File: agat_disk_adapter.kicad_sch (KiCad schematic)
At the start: 14 parts, among them J1 КОНТРОЛЛЕР, J2_A1 ИЗОТ, J2_B2 ИЗОТ, J3 DISK II, J4 GOTEK, J5 Питание GOTEK, J6 ВБ, J7 Джамперы, J8 ВБ2, J9_A1 КОНТРОЛЛЕР, J9_B2 КОНТРОЛЛЕР

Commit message: add second FDC connector - Eltra male for standard Agat FDD cable
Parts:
- removed R2: 0, Resistor_SMD:R_1206_3216Metric, symbol Device:R
- added J9: PIN_32, Connector_PinHeader_2.54mm:PinHeader_1x02_P2.54mm_Horizontal, symbol Connector:Conn_01x02_Pin
- renumbered R3 to R2
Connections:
- net PH1: now also J9.2 (Pin_2)
- net PIN_32: now reaches J4.32 (Pin_32), R2.2
- net PIN_32: now also J9.1 (Pin_1)
- net DS2 renamed DE2
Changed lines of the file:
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@@
 	)
 	(junction
+		(at 91.44 175.26)
+		(diameter 0)
+		(color 0 0 0 0)
+	)
+	(junction
 		(at 91.44 106.68)
 		(diameter 0)
@@
 	)
 	(junction
-		(at 91.44 166.878)
-		(diameter 0)
-		(color 0 0 0 0)
-	)
-	(junction
 		(at 81.28 191.643)
 		(diameter 0)
@@
 	(wire
 		(pts
-			(xy 91.44 166.878) (xy 91.44 177.038)
+			(xy 91.44 166.878) (xy 91.44 175.26)
 		)
 		(stroke
@@
 	(wire
 		(pts
+			(xy 91.44 175.26) (xy 91.44 177.038)
+		)
+		(stroke
+			(width 0)
+			(type default)
+		)
+	)
+	(wire
+		(pts
 			(xy 60.96 191.643) (xy 60.96 189.738)
 		)
@@
 	(wire
 		(pts
+			(xy 106.68 180.34) (xy 106.68 175.26)
+		)
+		(stroke
+			(width 0)
+			(type default)
+		)
+	)
+	(wire
+		(pts
 			(xy 78.74 18.415) (xy 78.74 25.4)
 		)
@@
 	(wire
 		(pts
+			(xy 91.44 175.26) (xy 104.14 175.26)
+		)
+		(stroke
+			(width 0)
+			(type default)
+		)
+	)
+	(wire
+		(pts
 			(xy 29.21 37.465) (xy 29.21 34.925)
 		)
@@
 		)
 	)
+	(label "PIN_32"
+		(at 91.948 175.26 0)
+		(effects
+			(font
+				(size 1.27 1.27)
+			)
+			(justify left bottom)
+		)
+	)
 	(label "EN1"
 		(at 78.74 66.675 270)
@@
 		)
 	)
-	(label "+5"
-		(at 80.518 166.878 0)
+	(label "PH1"
+		(at 106.68 180.34 0)
 		(effects
 			(font
@@
 		)
 	)
-	(label "DS2"
+	(label "DE2"
 		(at 99.06 121.285 90)
 		(effects
@@
 	)
 	(symbol
-		(lib_id "Device:R")
-		(at 87.63 166.878 90)
-		(unit 1)
-		(body_style 1)
-		(exclude_from_sim no)
-		(in_bom yes)
-		(on_board yes)
-		(in_pos_files yes)
-		(dnp no)
-		(property "Reference" "R2"
-			(at 86.36 164.592 90)
-			(show_name no)
-			(do_not_autoplace no)
-			(effects
-				(font
-					(size 1.27 1.27)
-				)
-			)
-		)
-		(property "Value" "0"
-			(at 89.662 164.592 90)
-			(show_name no)
-			(do_not_autoplace no)
-			(effects
-				(font
-					(size 1.27 1.27)
-				)
-			)
-		)
-		(property "Footprint" "Resistor_SMD:R_1206_3216Metric"
-			(at 87.63 168.656 90)
-			(hide yes)
-			(show_name no)
-			(do_not_autoplace no)
-			(effects
-				(font
-					(size 1.27 1.27)
-				)
-			)
-		)
-		(property "Datasheet" ""
-			(at 87.63 166.878 0)
-			(hide yes)
-			(show_name no)
-			(do_not_autoplace no)
-			(effects
-				(font
-					(size 1.27 1.27)
-				)
-			)
-		)
-		(property "Description" "Resistor"
-			(at 87.63 166.878 0)
-			(hide yes)
-			(show_name no)
-			(do_not_autoplace no)
-			(effects
-				(font
-					(size 1.27 1.27)
-				)
-			)
-		)
-		(pin "2"
-		)
-		(pin "1"
-		)
-		(instances
-			(project "agat_disk_adapter"
-				(path "/e6908ff4-84b7-4cdb-b4c1-fd2e829eca09"
-					(reference "R2")
-					(unit 1)
-				)
-			)
-		)
-	)
-	(symbol
 		(lib_id "power:GND")
 		(at 95.885 38.1 0)
@@
 	)
 	(symbol
+		(lib_id "Connector:Conn_01x02_Pin")
+		(at 104.14 170.18 90)
+		(mirror x)
+		(unit 1)
+		(body_style 1)
+		(exclude_from_sim no)
+		(in_bom yes)
+		(on_board yes)
+		(in_pos_files yes)
+		(dnp no)
+		(property "Reference" "J9"
+			(at 100.838 172.212 90)
+			(show_name no)
+			(do_not_autoplace no)
+			(effects
+				(font
+					(size 1.27 1.27)
+				)
+				(justify right)
+			)
+		)
+		(property "Value" "PIN_32"
+			(at 92.202 175.006 90)
+			(hide yes)
+			(show_name no)
+			(do_not_autoplace no)
+			(effects
+				(font
+					(size 1.27 1.27)
+				)
+				(justify right)
+			)
+		)
+		(property "Footprint" "Connector_PinHeader_2.54mm:PinHeader_1x02_P2.54mm_Horizontal"
+			(at 104.14 170.18 0)
+			(hide yes)
+			(show_name no)
+			(do_not_autoplace no)
+			(effects
+				(font
+					(size 1.27 1.27)
+				)
+			)
+		)
+		(property "Datasheet" ""
+			(at 104.14 170.18 0)
+			(hide yes)
+			(show_name no)
+			(do_not_autoplace no)
+			(effects
+				(font
+					(size 1.27 1.27)
+				)
+			)
+		)
+		(property "Description" "Generic connector, single row, 01x02, script generated"
+			(at 104.14 170.18 0)
+			(hide yes)
+			(show_name no)
+			(do_not_autoplace no)
+			(effects
+				(font
+					(size 1.27 1.27)
+				)
+			)
+		)
+		(pin "1"
+		)
+		(pin "2"
+		)
+		(instances
+			(project "agat_disk_adapter"
+				(path "/e6908ff4-84b7-4cdb-b4c1-fd2e829eca09"
+					(reference "J9")
+					(unit 1)
+				)
+			)
+		)
+	)
+	(symbol
 		(lib_id "Connector_Generic:Conn_02x05_Odd_Even")
 		(at 34.29 114.935 0)
@@
 		(in_pos_files yes)
 		(dnp yes)
-		(property "Reference" "R3"
+		(property "Reference" "R2"
 			(at 93.726 164.592 90)
 			(show_name no)
@@
 			(project "agat_disk_adapter"
 				(path "/e6908ff4-84b7-4cdb-b4c1-fd2e829eca09"
-					(reference "R3")
+					(reference "R2")
 					(unit 1)
 				)

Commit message: set clearance to 0.22, adjust all traces, align J5 "fan", add J10 "-12->DE2"
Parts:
- added J10: PIN_32, Connector_PinHeader_2.54mm:PinHeader_1x02_P2.54mm_Horizontal, symbol Connector:Conn_01x02_Pin
- added R3: 0, Resistor_SMD:R_1206_3216Metric, symbol Device:R
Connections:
- net +5: now also J6.8 (Pin_8)
- net -12: now also J10.2 (Pin_2), R3.1
- net DE2: now also J6.10 (Pin_10), J6.2 (Pin_2), J6.6 (Pin_6), J10.1 (Pin_1), R3.2
- net GND: now also J6.4 (Pin_4)
- net EN1 renamed DE1
- removed net EN2: J6.4 (Pin_4), J6.8 (Pin_8)
- net EN_J2 renamed DE_J2
- net DE_J2: no longer J6.2 (Pin_2)
- net EN_J3 renamed DE_J3
- net DE_J3: no longer J6.6 (Pin_6)
- net EN_J4 renamed DE_J4
- net DE_J4: no longer J6.10 (Pin_10)
- net PIN_32 renamed G32
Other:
- moved on the sheet: J6, J8, J9, R2

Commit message: add solder drop jumper footprint; add led resistor; thermal-relief +5 trace
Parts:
- added R4: 680R, Resistor_THT:R_Axial_DIN0207_L6.3mm_D2.5mm_P10.16mm_Horizontal, symbol Device:R
- added R5: 680R, agat_disk_adapter:0R_1206_solder_drop_jumper, symbol Device:R
- J3: value DISK II -> IDC‐20; Function (none) -> APPLE2
- R1: footprint Resistor_SMD:R_1206_3216Metric -> agat_disk_adapter:0R_1206_solder_drop_jumper
- R2: value 0 -> 0R; footprint Resistor_SMD:R_1206_3216Metric -> agat_disk_adapter:0R_1206_solder_drop_jumper
- R3: value 0 -> 0R; Function (none) -> DE2 -> -12
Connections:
- net +5: now also R4.2, R5.1; no longer J6.8 (Pin_8)
- net DE2: now also R3.1; no longer R3.2
- net G32: now also R2.1; no longer R2.2
- net PH1: now also R2.2; no longer R2.1
- net -12 renamed -12|DE2
- net -12|DE2: now also R3.2; no longer R3.1
- new net LED+: J6.8 (Pin_8), R4.1, R5.2
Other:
- moved on the sheet: R2, R3

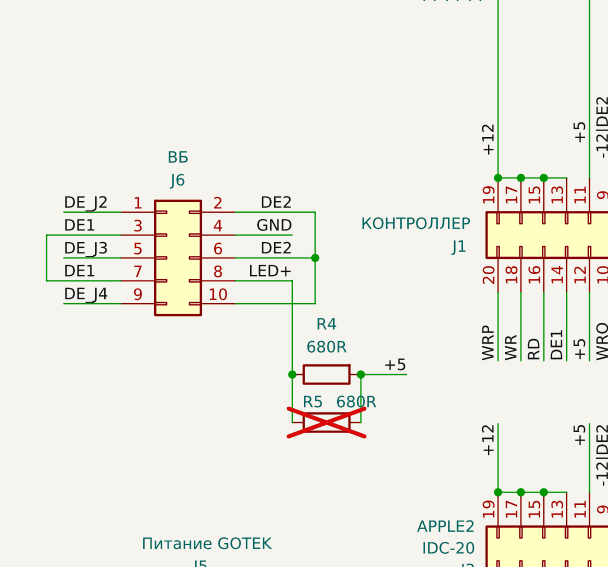
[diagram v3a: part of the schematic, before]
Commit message: flip front panel DE connector for better tracing
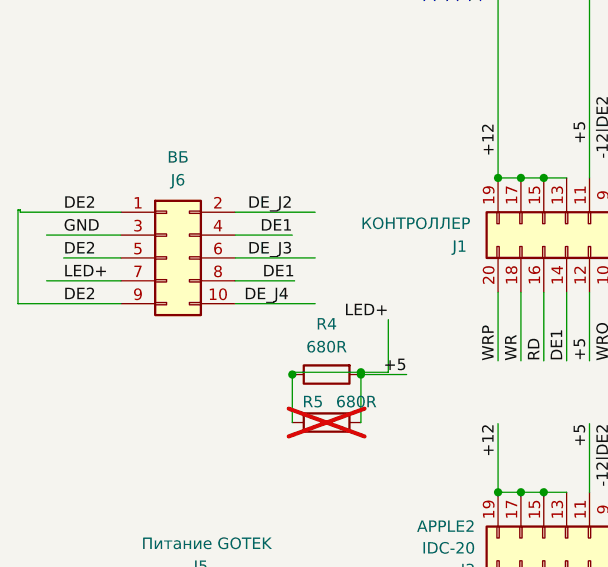
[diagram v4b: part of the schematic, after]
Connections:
- net +5: now also J6.7 (Pin_7), R4.1, R5.2
- net DE1: now also J6.4 (Pin_4), J6.8 (Pin_8); no longer J6.3 (Pin_3), J6.7 (Pin_7)
- net DE2: now also J6.1 (Pin_1), J6.5 (Pin_5), J6.9 (Pin_9); no longer J6.10 (Pin_10), J6.2 (Pin_2), J6.6 (Pin_6)
- net DE_J2: now also J6.2 (Pin_2); no longer J6.1 (Pin_1)
- net DE_J3: now also J6.6 (Pin_6); no longer J6.5 (Pin_5)
- net DE_J4: now also J6.10 (Pin_10); no longer J6.9 (Pin_9)
- net GND: now also J6.3 (Pin_3); no longer J6.4 (Pin_4)
- removed net LED+: J6.8 (Pin_8), R4.1, R5.2
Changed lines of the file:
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@@
-	)
-	(junction
-		(at 50.8 115.57)
-		(diameter 0)
-		(color 0 0 0 0)
 	)
 	(junction
@@
 	(junction
 		(at 41.91 34.925)
+		(diameter 0)
+		(color 0 0 0 0)
+	)
+	(junction
+		(at 55.88 128.27)
 		(diameter 0)
 		(color 0 0 0 0)
@@
 	(wire
 		(pts
+			(xy 48.514 118.11) (xy 41.91 118.11)
+		)
+		(stroke
+			(width 0)
+			(type default)
+		)
+	)
+	(wire
+		(pts
 			(xy 76.2 191.643) (xy 76.2 189.738)
 		)
@@
 	(wire
 		(pts
+			(xy 17.78 110.236) (xy 17.78 120.65)
+		)
+		(stroke
+			(width 0)
+			(type default)
+		)
+	)
+	(wire
+		(pts
 			(xy 83.82 191.643) (xy 83.82 189.738)
 		)
@@
 	(wire
 		(pts
-			(xy 48.26 118.11) (xy 41.91 118.11)
-		)
-		(stroke
-			(width 0)
-			(type default)
-		)
-	)
-	(wire
-		(pts
 			(xy 104.14 167.64) (xy 104.14 170.18)
 		)
@@
 	(wire
 		(pts
-			(xy 50.8 115.57) (xy 50.8 120.65)
-		)
-		(stroke
-			(width 0)
-			(type default)
-		)
-	)
-	(wire
-		(pts
 			(xy 91.44 38.1) (xy 93.98 38.1)
 		)
@@
 	(wire
 		(pts
+			(xy 17.78 110.236) (xy 18.034 110.236)
+		)
+		(stroke
+			(width 0)
+			(type default)
+		)
+	)
+	(wire
+		(pts
 			(xy 81.28 18.415) (xy 81.28 25.4)
 		)
@@
 	(wire
 		(pts
-			(xy 48.26 118.11) (xy 48.26 128.524)
+			(xy 58.928 122.428) (xy 58.928 128.27)
 		)
 		(stroke
@@
 	(wire
 		(pts
-			(xy 50.8 110.49) (xy 50.8 115.57)
-		)
-		(stroke
-			(width 0)
-			(type default)
-		)
-	)
-	(wire
-		(pts
 			(xy 91.44 119.38) (xy 91.44 127)
 		)
@@
 	(wire
 		(pts
-			(xy 22.86 120.65) (xy 29.21 120.65)
-		)
-		(stroke
-			(width 0)
-			(type default)
-		)
-	)
-	(wire
-		(pts
 			(xy 76.2 66.675) (xy 76.2 73.66)
 		)
@@
 	(wire
 		(pts
+			(xy 58.928 128.27) (xy 55.88 128.27)
+		)
+		(stroke
+			(width 0)
+			(type default)
+		)
+	)
+	(wire
+		(pts
 			(xy 86.36 191.643) (xy 86.36 189.738)
 		)
@@
 	(wire
 		(pts
-			(xy 22.86 110.49) (xy 29.21 110.49)
-		)
-		(stroke
-			(width 0)
-			(type default)
-		)
-	)
-	(wire
-		(pts
 			(xy 71.12 133.985) (xy 71.12 141.605)
 		)
@@
 	(wire
 		(pts
+			(xy 18.034 110.236) (xy 18.034 110.49)
+		)
+		(stroke
+			(width 0)
+			(type default)
+		)
+	)
+	(wire
+		(pts
 			(xy 86.36 141.605) (xy 88.9 141.605)
 		)
@@
 	(wire
 		(pts
+			(xy 18.034 110.49) (xy 29.21 110.49)
+		)
+		(stroke
+			(width 0)
+			(type default)
+		)
+	)
+	(wire
+		(pts
 			(xy 55.88 128.27) (xy 55.88 128.524)
 		)
@@
 	(wire
 		(pts
+			(xy 55.88 128.27) (xy 48.26 128.27)
+		)
+		(stroke
+			(width 0)
+			(type default)
+		)
+	)
+	(wire
+		(pts
+			(xy 48.26 128.27) (xy 48.26 128.524)
+		)
+		(stroke
+			(width 0)
+			(type default)
+		)
+	)
+	(wire
+		(pts
 			(xy 91.44 106.68) (xy 93.98 106.68)
 		)
@@
 	(wire
 		(pts
+			(xy 17.78 120.65) (xy 29.21 120.65)
+		)
+		(stroke
+			(width 0)
+			(type default)
+		)
+	)
+	(wire
+		(pts
 			(xy 76.2 18.415) (xy 76.2 25.4)
 		)
@@
 	(wire
 		(pts
-			(xy 20.955 113.03) (xy 20.955 118.11)
-		)
-		(stroke
-			(width 0)
-			(type default)
-		)
-	)
-	(wire
-		(pts
 			(xy 80.518 166.878) (xy 83.82 166.878)
 		)
@@
 	(wire
 		(pts
+			(xy 41.91 120.65) (xy 50.8 120.65)
+		)
+		(stroke
+			(width 0)
+			(type default)
+		)
+	)
+	(wire
+		(pts
 			(xy 91.44 170.18) (xy 100.33 170.18)
 		)
@@
 	(wire
 		(pts
-			(xy 41.91 120.65) (xy 50.8 120.65)
-		)
-		(stroke
-			(width 0)
-			(type default)
-		)
-	)
-	(wire
-		(pts
 			(xy 66.04 170.18) (xy 66.04 177.038)
 		)
@@
 		)
 	)
-	(label "DE_J4"
+	(label "DE2"
 		(at 22.86 120.65 0)
 		(effects
@@
 		)
 	)
-	(label "GND"
+	(label "DE1"
 		(at 48.26 113.03 180)
 		(effects
@@
 		)
 	)
-	(label "DE2"
+	(label "DE_J2"
 		(at 48.26 110.49 180)
 		(effects
@@
 		)
 	)
+	(label "DE_J4"
+		(at 42.926 120.65 0)
+		(effects
+			(font
+				(size 1.27 1.27)
+			)
+			(justify left bottom)
+		)
+	)
 	(label "-12|DE2"
 		(at 93.98 129.54 0)
@@
 		)
 	)
-	(label "DE_J2"
+	(label "DE2"
 		(at 22.86 110.49 0)
 		(effects
@@
 		)
 	)
-	(label "DE1"
+	(label "GND"
 		(at 22.86 113.03 0)
 		(effects
@@
 		)
 	)
-	(label "DE2"
+	(label "DE_J3"
 		(at 48.26 115.57 180)
 		(effects
@@
 		)
 	)
-	(label "DE_J3"
+	(label "DE2"
 		(at 22.86 115.57 0)
 		(effects
@@
 		)
 	)
+	(label "DE1"
+		(at 48.514 118.11 180)
+		(effects
+			(font
+				(size 1.27 1.27)
+			)
+			(justify right bottom)
+		)
+	)
 	(label "RD"
 		(at 76.2 66.675 270)
@@
 		)
 	)
-	(label "DE1"
+	(label "LED+"
 		(at 22.86 118.11 0)
 		(effects
@@
 	)
 	(label "LED+"
-		(at 48.26 118.11 180)
-		(effects
-			(font
+		(at 58.928 122.428 180)
+		(effects
+			(font
